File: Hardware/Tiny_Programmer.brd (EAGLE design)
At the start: 59.7 x 15.2 mm, 31 parts, among them Q1 16MHz, U1 ATTINY84, X1 USB-A-H

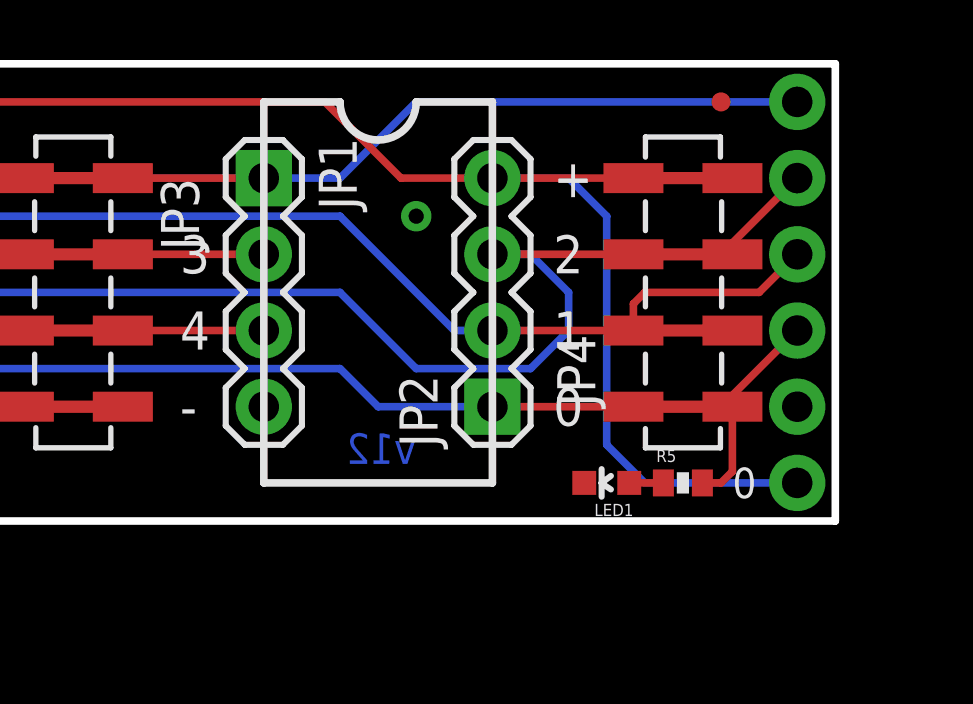
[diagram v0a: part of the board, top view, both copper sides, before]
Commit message: Added labels to each SIP pin. Moved 0 indicator.
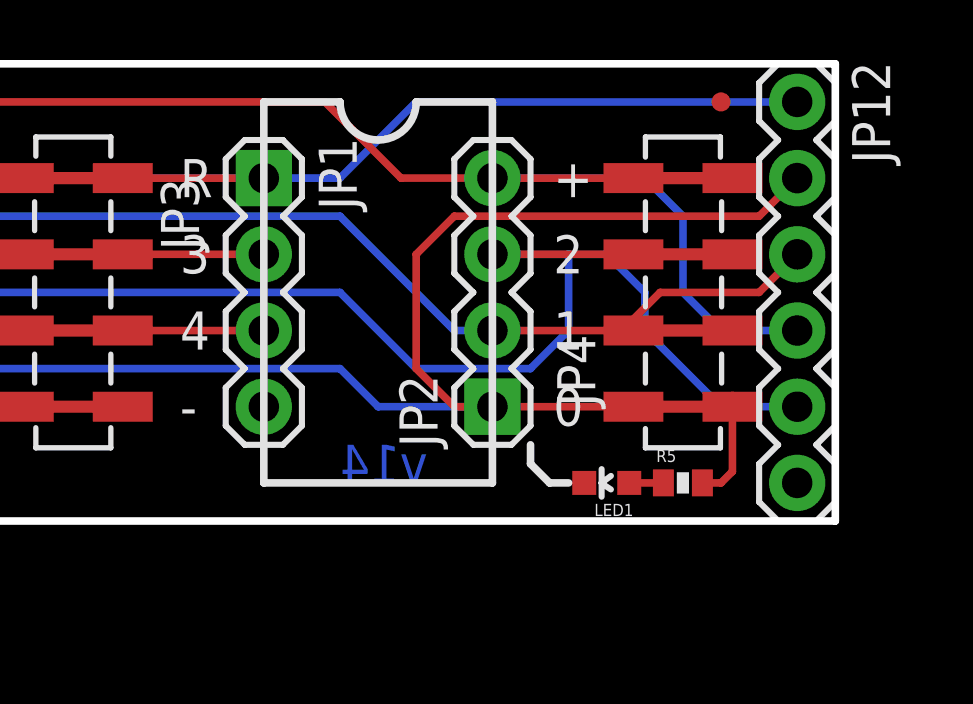
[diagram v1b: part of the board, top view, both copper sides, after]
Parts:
- flipped JP12 to the top
- renumbered JP10 to JP12
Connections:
- net GND: now also JP12.6; no longer JP12.5
- net MOSI: now also JP12.2; no longer JP12.4
- net SCK: now also JP12.5; no longer JP12.2
- net VCC: now also JP12.4; no longer JP12.6
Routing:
- net MOSI: track 64.9 -> 82.5 mm
- net SCK: track 58.0 -> 65.8 mm
- net VCC: track 86.5 -> 81.5 mm
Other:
- board text added: "5V"
- board text added: "GND"
- board text added: "MI"
- board text added: "MO"
- board text added: "R"
- board text added: "SCK"
- board text added: "v14"
- board text removed: "v12"
